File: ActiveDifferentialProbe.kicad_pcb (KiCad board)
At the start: 2 copper layers, 51 x 26 mm, 46 parts, among them J1 Conn_01x01, J16 Conn_01x01, J18 Conn_01x01, J19 Conn_01x01, J2 Conn_01x01, J20 Conn_01x01, J21 Conn_01x01, J22 Conn_01x01, J23 Conn_01x01, J25 Conn_Coaxial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

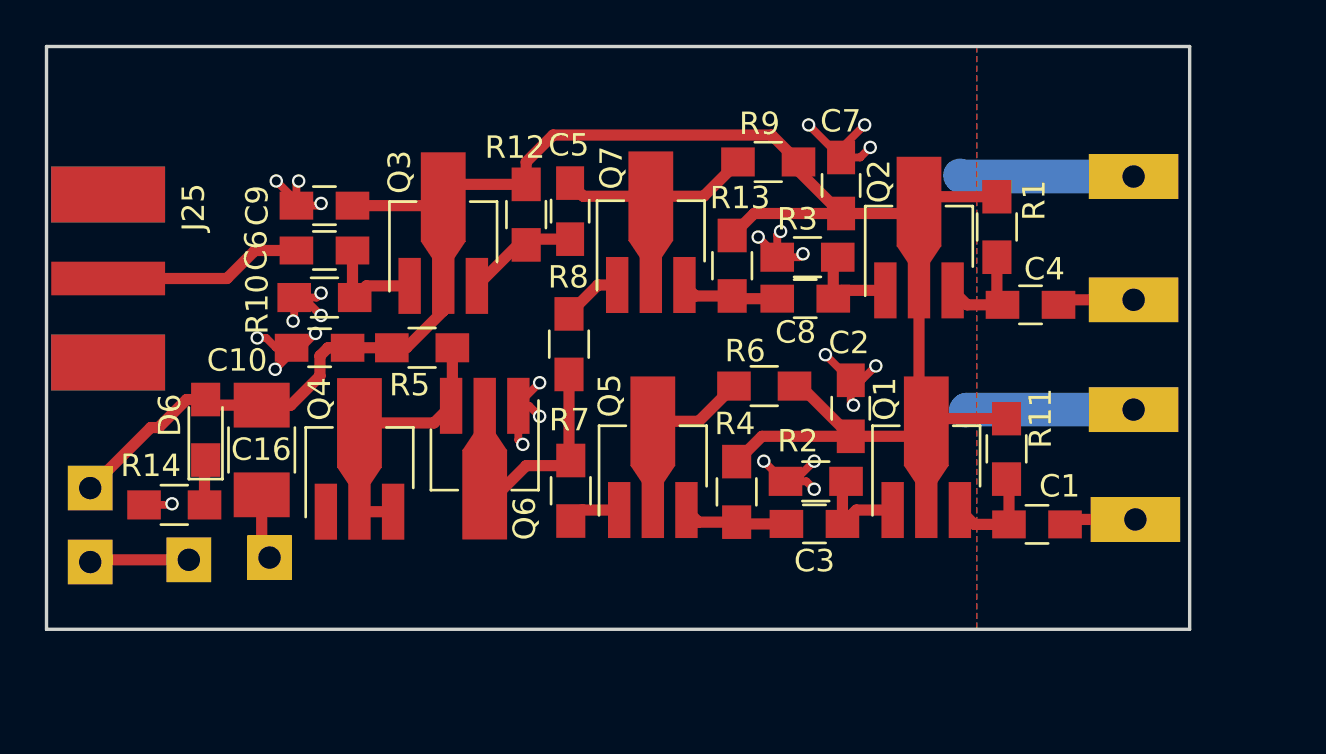
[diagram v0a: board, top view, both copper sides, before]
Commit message: Added LCSC parts, fixed symbol, added decoupling resistors
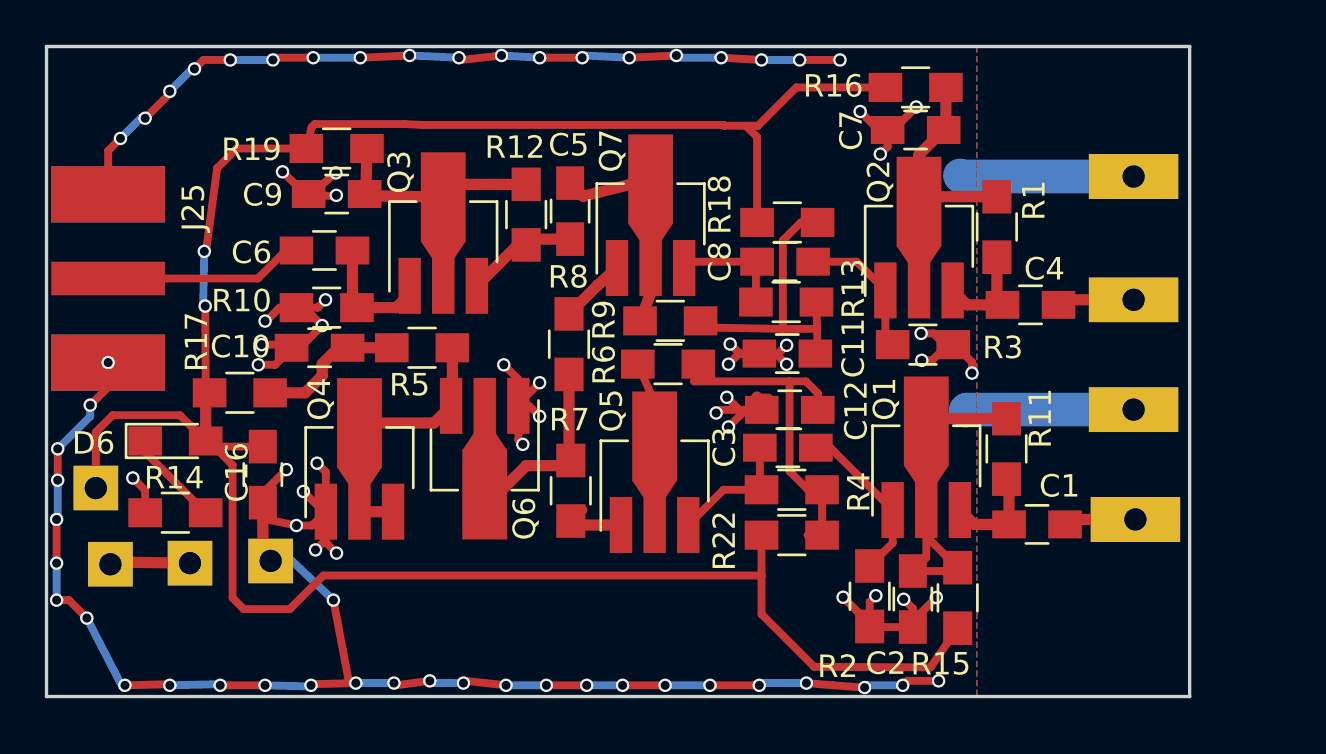
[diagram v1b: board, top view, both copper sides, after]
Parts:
- added C11: 100 nF, Capacitors_SMD:C_0805_HandSoldering, F.Cu at (96.0, 91.7)
- added C12: 100 nF, Capacitors_SMD:C_0805_HandSoldering, F.Cu at (96.2, 94.2)
- added R15: 10R, Resistors_SMD:R_0805_HandSoldering, F.Cu at (103.7, 102.6)
- added R16: 10R, Resistors_SMD:R_0805_HandSoldering, F.Cu at (101.8, 79.8)
- added R17: 10R, Resistors_SMD:R_0805_HandSoldering, F.Cu at (71.6, 93.5)
- added R18: 10R, Resistors_SMD:R_0805_HandSoldering, F.Cu at (96.0, 85.8)
- added R19: 10R, Resistors_SMD:R_0805_HandSoldering, F.Cu at (75.9, 82.5)
- added R22: 10R, Resistors_SMD:R_0805_HandSoldering, F.Cu at (96.2, 99.8)
- C16: footprint Capacitors_SMD:C_1210_HandSoldering -> Capacitors_SMD:C_0805_HandSoldering
- moved C2 8.95 mm to (101.7, 102.7), turned to 90 degrees
- moved R9 8.33 mm to (90.8, 90.2)
- moved R3 6.46 mm to (102.1, 91.3), turned to 0 degrees
- moved R2 5.66 mm to (99.7, 102.5), turned to 270 degrees
- moved R6 4.40 mm to (90.7, 92.2)
- moved C7 4.15 mm to (101.8, 81.7), turned to 0 degrees
- moved C3 3.60 mm to (96.1, 95.9)
- moved R13 2.90 mm to (96.0, 89.4), turned to 0 degrees
- moved J20 2.78 mm to (91.8, 104.7)
- moved J21 2.65 mm to (81.7, 104.7)
- moved R4 2.46 mm to (96.2, 97.8), turned to 0 degrees
- moved C8 1.88 mm to (96.0, 87.6)
- moved D6 1.44 mm to (68.8, 95.6), turned to 0 degrees
- moved C16 1.10 mm to (72.7, 97.1)
- moved J3 0.91 mm to (65.8, 101.1)
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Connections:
- C10 pad 1: +9V -> Net-(C10-Pad1)
- C2 pad 2: +9V -> Net-(C2-Pad2)
- C7 pad 2: +9V -> Net-(C7-Pad2)
- C9 pad 2: +9V -> Net-(C9-Pad2)
- Q1 pad 2: +9V -> Net-(C2-Pad2)
- Q2 pad 2: +9V -> Net-(C7-Pad2)
- Q3 pad 2: +9V -> Net-(C9-Pad2)
- R1 pad 2: +9V -> Net-(C7-Pad2)
- R11 pad 2: +9V -> Net-(C2-Pad2)
- R12 pad 2: +9V -> Net-(C9-Pad2)
- R13 pad 2: +9V -> Net-(C11-Pad2)
- R4 pad 2: +9V -> Net-(C12-Pad2)
- R5 pad 1: +9V -> Net-(C10-Pad1)
- R6 pad 2: +9V -> Net-(C12-Pad2)
- R9 pad 2: +9V -> Net-(C11-Pad2)
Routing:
- net GND: track 53.6 -> 183.5 mm, vias 25 -> 84
- net Net-(C2-Pad2): track 0.00 -> 17.3 mm
- net Net-(C12-Pad2): track 0.00 -> 16.0 mm
- net Net-(C7-Pad2): track 0.00 -> 16.0 mm
- net Net-(C9-Pad2): track 0.00 -> 14.6 mm
- net Net-(C11-Pad2): track 0.00 -> 13.5 mm
- net +9V: track 93.2 -> 106.0 mm, vias 0 -> 2
- net Net-(C10-Pad1): track 0.00 -> 6.57 mm
- net Net-(C3-Pad2): track 4.46 -> 7.50 mm
- net Net-(C8-Pad2): track 4.41 -> 6.86 mm
- net Net-(D6-Pad1): track 2.02 -> 4.32 mm
- net Net-(C5-Pad2): track 12.3 -> 10.3 mm
- net Net-(C6-Pad1): track 8.92 -> 10.4 mm
- net Net-(C3-Pad1): track 4.72 -> 6.01 mm
- net Net-(C6-Pad2): track 4.81 -> 5.74 mm
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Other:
- board size 51 x 26 mm -> 51 x 29 mm

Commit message: Changed to 2SC3356
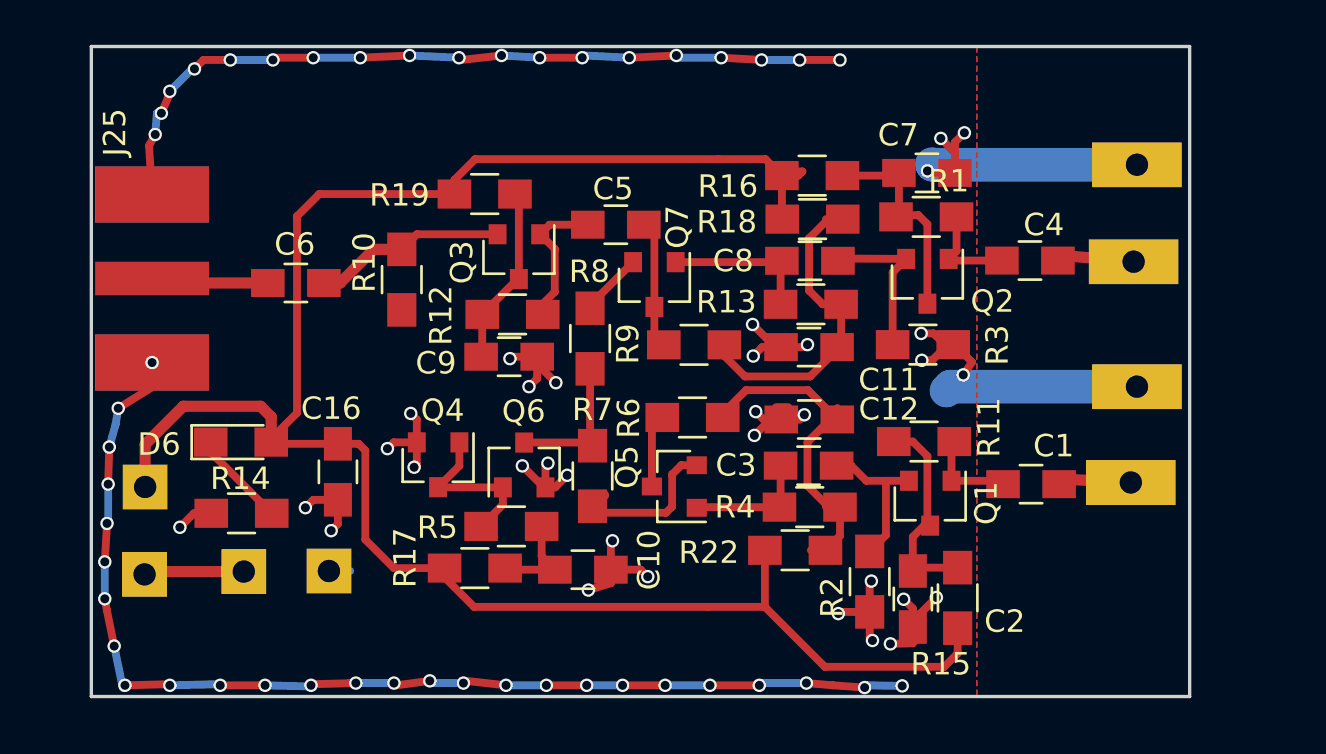
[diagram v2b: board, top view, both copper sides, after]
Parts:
- Q1, Q2, Q3, Q4, Q5, Q6, Q7: value 2SC3357 -> 2SC3356; footprint TO_SOT_Packages_SMD:SOT-89-3_Handsoldering -> TO_SOT_Packages_SMD:SOT-23
- moved C10 15.4 mm to (86.9, 101.3), turned to 0 degrees
- moved R17 13.1 mm to (82.1, 101.3)
- moved C9 10.6 mm to (83.6, 91.8), turned to 180 degrees
- moved R5 8.91 mm to (83.7, 99.4), turned to 180 degrees
- moved R19 6.91 mm to (82.5, 84.6)
- moved R16 6.06 mm to (97.2, 83.8)
- moved R12 4.49 mm to (83.8, 90.0), turned to 180 degrees
- moved R11 3.69 mm to (102.2, 95.6), turned to 180 degrees
- moved R10 3.58 mm to (78.8, 88.4), turned to 270 degrees
- moved Q4 3.51 mm to (80.5, 96.7), turned to 270 degrees
- moved Q3 3.44 mm to (84.1, 87.4), turned to 270 degrees
- moved C16 3.35 mm to (76.0, 97.0)
- moved R1 3.18 mm to (102.2, 85.6), turned to 180 degrees
- moved R14 2.95 mm to (71.7, 98.8)
- moved D6 2.93 mm to (71.7, 95.7)
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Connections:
- Q1 pad 1: Net-(C3-Pad2) -> Net-(C1-Pad1)
- Q1 pad 2: Net-(C2-Pad2) -> Net-(C3-Pad2)
- Q1 pad 3: Net-(C1-Pad1) -> Net-(C2-Pad2)
- Q2 pad 1: Net-(C8-Pad2) -> Net-(C4-Pad1)
- Q2 pad 2: Net-(C7-Pad2) -> Net-(C8-Pad2)
- Q2 pad 3: Net-(C4-Pad1) -> Net-(C7-Pad2)
- Q3 pad 1: Net-(C6-Pad2) -> Net-(C5-Pad1)
- Q3 pad 2: Net-(C9-Pad2) -> Net-(C6-Pad2)
- Q3 pad 3: Net-(C5-Pad1) -> Net-(C9-Pad2)
- Q4 pad 1: GND -> Net-(Q4-Pad1)
- Q4 pad 2: Net-(Q4-Pad2) -> GND
- Q4 pad 3: Net-(Q4-Pad2) -> Net-(Q4-Pad1)
- Q5 pad 1: Net-(Q5-Pad1) -> Net-(C3-Pad1)
- Q5 pad 3: Net-(C3-Pad1) -> Net-(Q5-Pad3)
- Q6 pad 1: GND -> Net-(Q4-Pad1)
- Q6 pad 2: Net-(Q6-Pad2) -> GND
- Q6 pad 3: Net-(Q4-Pad2) -> Net-(Q6-Pad3)
- Q7 pad 1: Net-(Q7-Pad1) -> Net-(C8-Pad1)
- Q7 pad 2: Net-(C5-Pad2) -> Net-(Q7-Pad2)
- Q7 pad 3: Net-(C8-Pad1) -> Net-(C5-Pad2)
- R5 pad 2: Net-(Q4-Pad2) -> Net-(Q4-Pad1)
- R6 pad 1: Net-(Q5-Pad2) -> Net-(Q5-Pad3)
- R7 pad 1: Net-(Q6-Pad2) -> Net-(Q6-Pad3)
- R7 pad 2: Net-(Q5-Pad1) -> Net-(Q5-Pad2)
- R8 pad 1: Net-(Q7-Pad1) -> Net-(Q7-Pad2)
- R8 pad 2: Net-(Q6-Pad2) -> Net-(Q6-Pad3)
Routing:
- net GND: track 183.5 -> 157.8 mm, vias 84 -> 79
- net +9V: track 106.0 -> 89.8 mm, vias 2 -> 0
- net Net-(Q4-Pad2): track 14.1 -> 0.00 mm
- net Net-(Q6-Pad2): track 12.3 -> 0.00 mm
- net Net-(C2-Pad2): track 17.3 -> 9.70 mm
- net Net-(Q4-Pad1): track 0.00 -> 7.43 mm
- net Net-(Q6-Pad3): track 0.00 -> 7.02 mm
- net Net-(C9-Pad2): track 14.6 -> 8.06 mm
- net Net-(C7-Pad2): track 16.0 -> 10.0 mm
- net Net-(C5-Pad2): track 10.3 -> 5.73 mm
- net Net-(Q5-Pad3): track 0.00 -> 3.92 mm
- net Net-(C6-Pad1): track 10.4 -> 6.70 mm
- net Net-(Q5-Pad1): track 3.01 -> 0.00 mm
- net Net-(Q7-Pad1): track 2.96 -> 0.00 mm
- net Net-(C6-Pad2): track 5.74 -> 8.65 mm
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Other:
- board size 51 x 29 mm -> 49 x 29 mm
- board text removed: "ACTIVE DIFFERENTIAL RF PROBE BY D MARKS KW4TI CC-BY-SA 4.0"

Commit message: Added LCSC part numbers, added cutout notched, added series base resistors to emitter followers
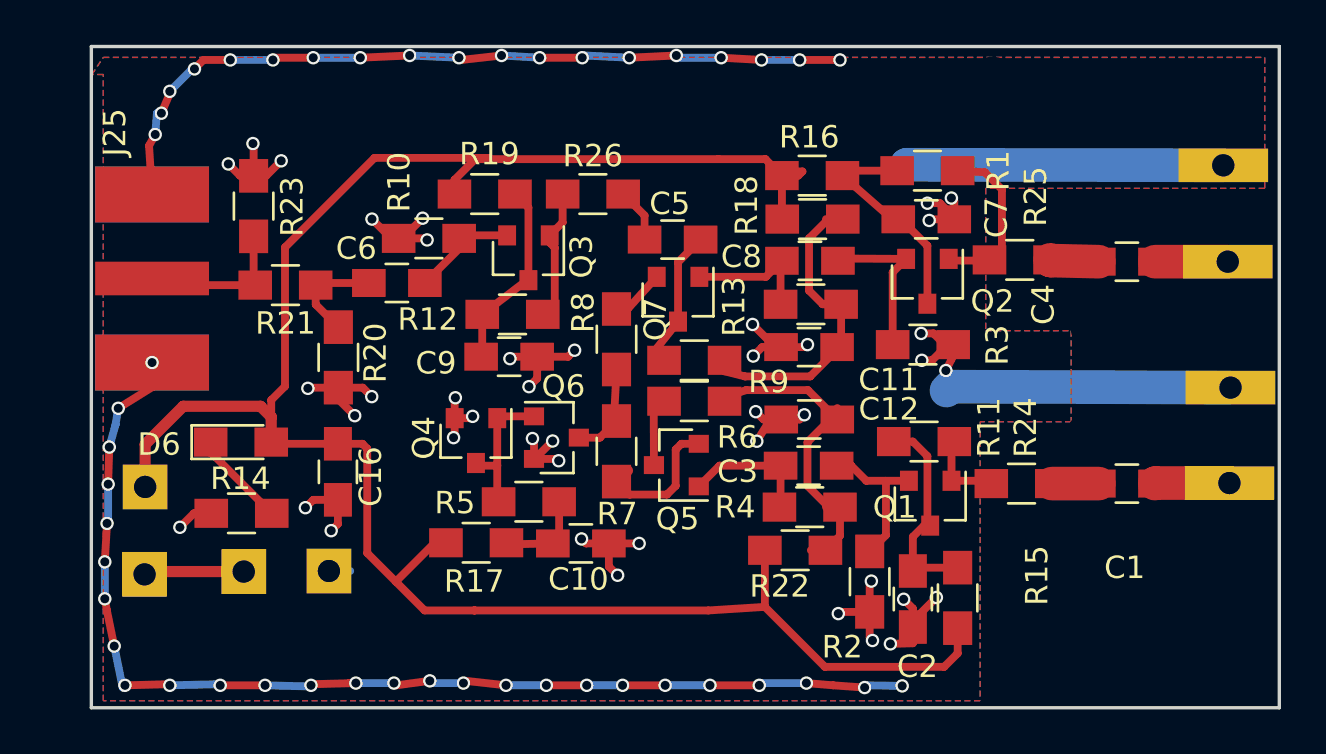
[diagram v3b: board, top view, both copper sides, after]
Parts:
- added J10: Conn_01x01, ActiveDifferentialProbe:BigSlot, F.Cu at (115.0, 95.3)
- added J11: Conn_01x01, ActiveDifferentialProbe:BigSlot, F.Cu at (109.5, 81.5)
- added J12: Conn_01x01, ActiveDifferentialProbe:BigSlot, F.Cu at (115.3, 99.3)
- added J13: Conn_01x01, ActiveDifferentialProbe:BigSlot, F.Cu at (105.4, 104.4)
- added J14: Conn_01x01, ActiveDifferentialProbe:BigSlot, F.Cu at (107.4, 99.3)
- added J15: Conn_01x01, ActiveDifferentialProbe:BigSlot, F.Cu at (105.2, 80.2)
- added J17: Conn_01x01, ActiveDifferentialProbe:BigSlot, F.Cu at (110.2, 85.3)
- added J24: Conn_01x01, ActiveDifferentialProbe:BigSlot, F.Cu at (110.2, 90.4)
- added J26: Conn_01x01, ActiveDifferentialProbe:BigSlot, F.Cu at (110.0, 95.2)
- added J27: Conn_01x01, ActiveDifferentialProbe:BigSlot, F.Cu at (110.7, 99.3)
- added J6: Conn_01x01, ActiveDifferentialProbe:BigSlot, F.Cu at (115.0, 90.4)
- added J7: Conn_01x01, ActiveDifferentialProbe:BigSlot, F.Cu at (115.0, 85.4)
- added J8: Conn_01x01, ActiveDifferentialProbe:BigSlot, F.Cu at (115.0, 81.5)
- added J9: Conn_01x01, ActiveDifferentialProbe:BigSlot, F.Cu at (105.4, 100.6)
- added R20: NC, Resistors_SMD:R_0805_HandSoldering, F.Cu at (76.0, 91.9)
- added R21: 0R, Resistors_SMD:R_0805_HandSoldering, F.Cu at (73.7, 88.6)
- added R23: NC, Resistors_SMD:R_0805_HandSoldering, F.Cu at (72.2, 85.1)
- added R24: 220R, Resistors_SMD:R_0805_HandSoldering, F.Cu at (106.5, 97.5)
- added R25: 220R, Resistors_SMD:R_0805_HandSoldering, F.Cu at (106.4, 87.5)
- added R26: 220R, Resistors_SMD:R_0805_HandSoldering, F.Cu at (87.4, 84.6)
- moved C6 4.50 mm to (78.6, 88.5)
- moved J1 4.40 mm to (115.8, 97.5)
- moved C4 4.33 mm to (111.2, 87.6)
- moved C1 4.28 mm to (111.2, 97.5)
- moved J5 4.20 mm to (115.7, 87.6)
- moved J16 4.17 mm to (115.8, 93.2)
- moved J4 3.85 mm to (115.5, 83.3)
- moved C5 2.62 mm to (90.9, 86.6)
- moved R10 2.20 mm to (80.1, 86.6), turned to 180 degrees
- moved C7 2.07 mm to (102.2, 85.7)
- moved R1 2.06 mm to (102.3, 83.5)
- moved Q4 2.01 mm to (82.2, 95.6)
- moved Q6 1.89 mm to (85.8, 95.5), turned to 0 degrees
- moved R7 1.53 mm to (88.4, 96.1)
- moved R5 1.35 mm to (84.5, 98.3)
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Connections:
- J25 pad 1: Net-(C6-Pad1) -> Net-(J25-Pad1)
- Q1 pad 1: Net-(C1-Pad1) -> Net-(Q1-Pad1)
- Q2 pad 1: Net-(C4-Pad1) -> Net-(Q2-Pad1)
- Q3 pad 1: Net-(C5-Pad1) -> Net-(Q3-Pad1)
- R1 pad 1: Net-(C4-Pad1) -> Net-(Q2-Pad1)
- R11 pad 1: Net-(C1-Pad1) -> Net-(Q1-Pad1)
- R12 pad 1: Net-(C5-Pad1) -> Net-(Q3-Pad1)
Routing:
- net GND: track 157.8 -> 175.7 mm, vias 79 -> 88
- net Net-(Q2-Pad1): track 0.00 -> 8.23 mm
- net Net-(J25-Pad1): track 0.00 -> 7.21 mm
- net Net-(Q3-Pad1): track 0.00 -> 6.60 mm
- net +9V: track 89.8 -> 95.3 mm
- net Net-(Q1-Pad1): track 0.00 -> 4.16 mm
- net Net-(C5-Pad1): track 6.37 -> 2.43 mm
- net Net-(C6-Pad2): track 8.65 -> 4.82 mm
- net Net-(C4-Pad1): track 4.78 -> 2.55 mm
- net Net-(Q6-Pad3): track 7.02 -> 4.97 mm
- net Net-(C6-Pad1): track 6.70 -> 4.70 mm
- net Net-(C1-Pad1): track 4.16 -> 2.72 mm
- net Net-(Q4-Pad1): track 7.43 -> 6.43 mm
- net Net-(C9-Pad2): track 8.06 -> 8.82 mm
- net Net-(C7-Pad2): track 10.0 -> 10.7 mm
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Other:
- board size 49 x 29 mm -> 53 x 29.5 mm
- board text added: "ACTIVE RF DIFFERENTIAL PROBE BY D MARKS KW4TI CC-BY-SA 4.0"
